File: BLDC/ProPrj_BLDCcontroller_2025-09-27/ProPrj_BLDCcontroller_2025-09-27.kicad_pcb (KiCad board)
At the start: 4 copper layers, 40 x 40 mm, 51 parts, among them CN1 WAFER-GH1.25-7PLB, J1 Conn_01x01, J2 Conn_01x01, J3 Conn_01x01, J4 Conn_01x01, J5 Conn_01x01, SW2 SMD_4.2x3.2mm_h2.5mm, U1 SGM2019-3.3YN5G/TR, U10 AS5600-ASOM, U2 TPS54302DDCR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

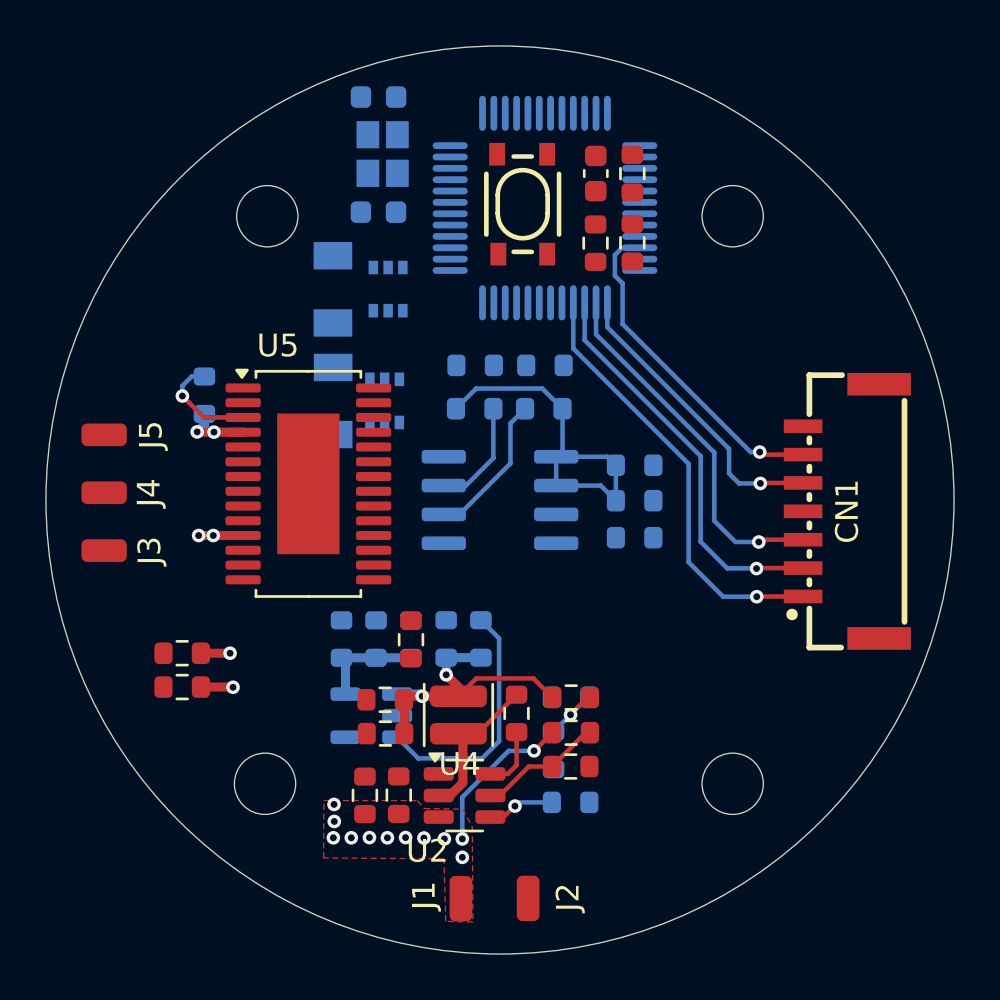
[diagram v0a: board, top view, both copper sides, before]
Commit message: 采样电阻位置调整
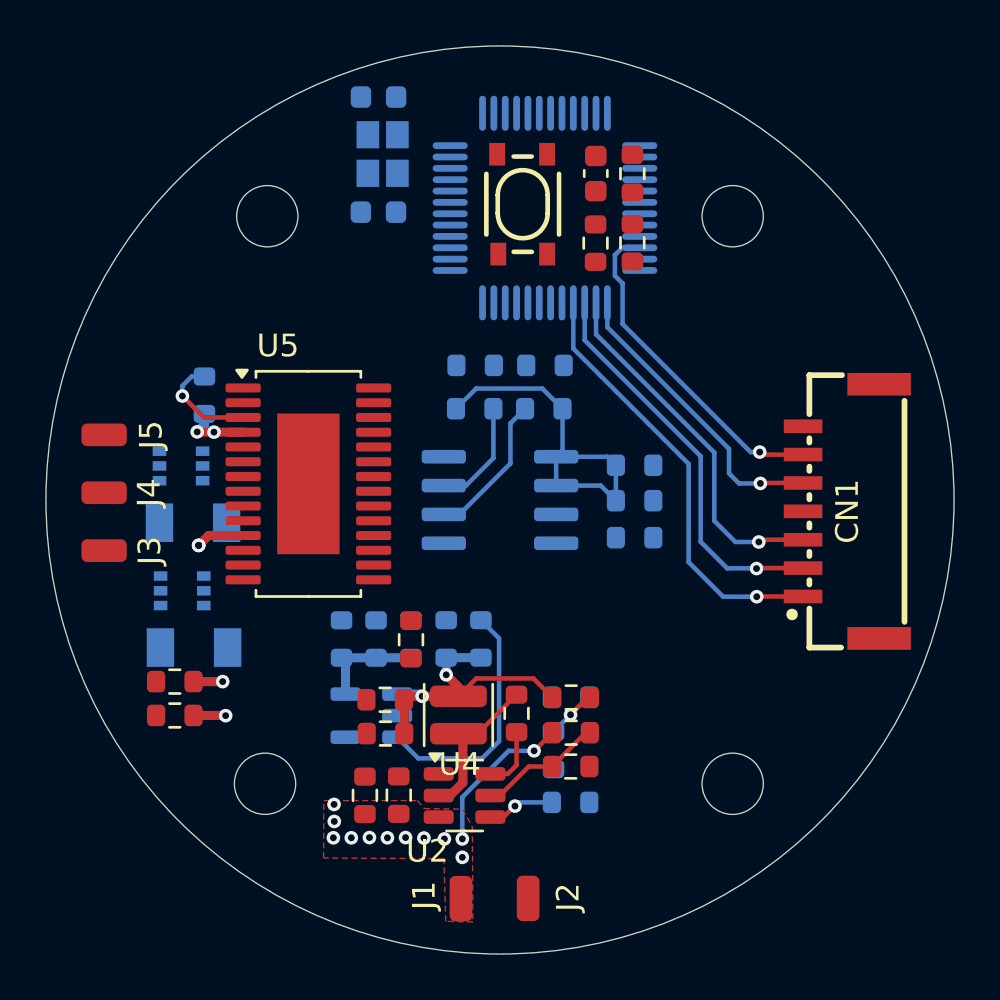
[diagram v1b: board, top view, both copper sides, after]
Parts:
- moved U8 16.9 mm to (201.5, 78.0), turned to 180 degrees
- moved U6 16.1 mm to (201.0, 75.5), turned to 0 degrees
- moved U7 9.41 mm to (200.9, 70.0), turned to 0 degrees
- moved U9 8.17 mm to (201.5, 72.5), turned to 180 degrees
- moved C17 1.29 mm to (200.7, 81.0)
- moved C18 1.29 mm to (200.7, 79.5)

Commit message: BLDC 更新
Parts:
- added C19: 10nF, Capacitor_SMD:C_0603_1608Metric, F.Cu at (202.4, 64.6)
- added R7: 0, SparkFun-Resistor:R_0603_1608Metric, B.Cu at (205.6, 75.4)
- C20: moved to F.Cu
- C22: value 100nF -> 1uF
- moved U6 9.36 mm to (200.4, 66.2)
- moved U8 9.36 mm to (200.9, 68.7)
- moved J3 5.10 mm to (197.6, 68.6), turned to -90 degrees
- moved J5 5.10 mm to (197.6, 73.7), turned to -90 degrees
- moved C6 3.70 mm to (213.3, 65.8), turned to 180 degrees
- moved R11 3.66 mm to (213.3, 67.3), turned to 180 degrees
- moved U7 3.57 mm to (201.1, 73.6)
- moved C1 2.77 mm to (216.7, 65.8), turned to 0 degrees
- moved R10 2.76 mm to (216.6, 67.3), turned to 180 degrees
- moved C21 1.85 mm to (211.8, 76.0)
- moved C15 1.64 mm to (208.7, 60.2), turned to 0 degrees
- moved Y1 1.63 mm to (208.7, 57.5)
- moved U9 1.52 mm to (200.9, 71.1)
- moved C16 1.42 mm to (208.8, 54.9)
- moved C20 0.36 mm to (201.6, 66.9)
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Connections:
- C21 pad 2: GND -> Net-(U5-COMPO#)
- C22 pad 1: unconnected-(C22-Pad1) -> GND
- C23 pad 1: unconnected-(C23-Pad1) -> GND
- J2 pad 1: /PGND -> GND
- J5 pad 1: /MOTOR3 -> MOTOR3
- R10 pad 2: /SCL -> /PB6
- R11 pad 1: /SDA -> /PB7
- U10 pad 4: unconnected-(U10-GND-Pad4) -> GND
- U10 pad 6: /SDA -> /PB7
- U10 pad 7: /SCL -> /PB6
- U3 pad 1: /VDD -> 3.3V
- U3 pad 23: /VSS -> GND
- U3 pad 24: /VDD -> 3.3V
- U3 pad 47: /VSS -> GND
- U3 pad 48: /VDD -> 3.3V
- U3 pad 8: /VSS -> GND
- U3 pad 9: /VDD -> 3.3V
- U5 pad 19: GND -> Net-(U5-COMPO#)
- U5 pad 22: unconnected-(U5-EN3-Pad22) -> /PB0
- U5 pad 24: unconnected-(U5-EN2-Pad24) -> /PA7
- U5 pad 26: unconnected-(U5-EN1-Pad26) -> /PA6
- U5 pad 9: OUT3 -> MOTOR3
- Y1 pad 2: Net-(Y1-Pad2) -> GND
- Y1 pad 4: Net-(Y1-Pad2) -> GND
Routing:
- net GND: track 0.00 -> 45.6 mm, vias 0 -> 15
- net /PB0: track 0.00 -> 33.1 mm, vias 0 -> 1
- net TIM1_CH1: track 0.00 -> 23.4 mm, vias 0 -> 1
- net TIM1_CH3: track 0.00 -> 22.1 mm, vias 0 -> 1
- net /PA7: track 0.00 -> 18.9 mm, vias 0 -> 3
- net /PA6: track 0.00 -> 16.8 mm, vias 0 -> 3
- net /PB7: track 0.00 -> 14.7 mm
- net TIM1_CH2: track 0.00 -> 11.2 mm, vias 0 -> 1
- net /PB6: track 0.00 -> 11.0 mm
- net /NRST: track 0.00 -> 8.83 mm, vias 0 -> 1
- net Net-(U10-PGO): track 0.00 -> 8.66 mm
- net /OSC_IN: track 0.00 -> 6.81 mm
- net /SDA: track 6.54 -> 0.00 mm
- net /OSC_OUT: track 0.00 -> 6.20 mm
- net 3.3V: track 20.9 -> 27.0 mm, vias 0 -> 6
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- added copper zone on F.Cu, net /PGND
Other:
- board text added: "N32G430C8L7"
